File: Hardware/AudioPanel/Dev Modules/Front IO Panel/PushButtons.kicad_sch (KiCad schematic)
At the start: 80 parts, among them CN501 4x 10nF, CN502 4x 10nF, CN503 4x 10nF, U501 74HC14, U502 74HC14, U503 74HC14, U504 74HC14, U505 74HC14, U506 74HC14, U507 MCP23017_ML, U508 74HC14, U509 74HC14, U510 74HC14, U511 74HC14, U512 74HC14, U513 74HC14

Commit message: IO Panel Progress
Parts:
- removed RN501, RN502, RN503, RN504, RN505, RN506, RN507, RN508, RN509, RN510, RN511, RN512: 10k, Resistor_THT:R_Array_SIP5, symbol Device:R_Network04_Split
- removed U507: MCP23017_ML, Package_DFN_QFN:QFN-28-1EP_6x6mm_P0.65mm_EP4.25x4.25mm, symbol Interface_Expansion:MCP23017_ML
- added C102: 22uF, Libraries:Worthington_C_0603, symbol Device:C_Small
- added C103: 100nF, Libraries:Worthington_C_0402, symbol Device:C_Small
- added CN504: 4x 10nF, symbol Device:C_Network04
- added D520: SP0504BAJT, Package_TO_SOT_SMD:SOT-353_SC-70-5, symbol Power_Protection:SP0504BAJT
- added PB513, PB514, PB515, PB516: KP_Switch, symbol Switch:SW_Push
- added R102, R501: 220Ω, Libraries:Worthington_R_0402, symbol Device:R_Small_US
- added RN501, RN502, RN503, RN504, RN505: 4k7, Resistor_SMD:R_Array_Convex_4x1206, symbol Library_MicSwitcher:R_Network04_Split
- added unit 7 of U503
- added U507, U520: SN74LV165ARGYR, Libraries:RGY16_2P55X2P05, symbol Libraries:74HC165
- added U514, U515, U516, U517, U518, U519: 74HC14, symbol AudioPanelLibrary:74HC14
- C501: value 100nF -> 22uF; footprint (none) -> Libraries:Worthington_C_0603
- C502: value 10uF -> 100nF; footprint (none) -> Libraries:Worthington_C_0402
- RN513, RN514, RN515: value 47k -> 4k7
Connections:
- net PB1 is gone; now on net ~{PB1}: D501.1 (K), PB501.2, RN513.2
- net PB10 is gone; now on net ~{PB10}: D503.3 (K), PB510.2, RN515.4
- net PB11 is gone; now on net ~{PB11}: D503.4 (K), PB511.2, RN515.6
- net PB12 is gone; now on net ~{PB12}: D503.5 (K), PB512.2, RN515.8
- net PB2 is gone; now on net ~{PB2}: D501.3 (K), PB502.2, RN513.4
- net PB3 is gone; now on net ~{PB3}: D501.4 (K), PB503.2, RN513.6
- net PB4 is gone; now on net ~{PB4}: D501.5 (K), PB504.2, RN513.8
- net PB5 is gone; now on net ~{PB5}: D502.1 (K), PB505.2, RN514.2
- net PB6 is gone; now on net ~{PB6}: D502.3 (K), PB506.2, RN514.4
- net PB7 is gone; now on net ~{PB7}: D502.4 (K), PB507.2, RN514.6
- net PB8 is gone; now on net ~{PB8}: D502.5 (K), PB508.2, RN514.8
- net PB9 is gone; now on net ~{PB9}: D503.1 (K), PB509.2, RN515.2
- net GND: now also C102.2, C103.2, CN504.1 (common), D520.2 (A), PB513.1, PB514.1, PB515.1, PB516.1, R102.2, U503.7 (GND), U507.8 (GND), U520.8 (GND)
- net VDD: now also C102.1, C103.1, RN505.1, RN505.3, RN505.5, RN505.7, U503.14 (VCC), U507.16 (VCC), U520.16 (VCC)
- net ~{PB10}: now also RN503.3; no longer U511.2
- net ~{PB11}: now also RN503.5; no longer U512.2
- net ~{PB12}: now also RN503.7; no longer U513.2
- net ~{PB1}: now also RN501.1; no longer U501.2
- net ~{PB2}: now also RN501.3; no longer U502.2
- net ~{PB3}: now also RN501.5; no longer U503.2
- net ~{PB4}: now also RN501.7; no longer U504.2
- net ~{PB5}: now also RN502.1; no longer U505.2
- net ~{PB6}: now also RN502.3; no longer U506.2
- net ~{PB7}: now also RN502.5; no longer U508.2
- net ~{PB8}: now also RN502.7; no longer U509.2
- net ~{PB9}: now also RN503.1; no longer U510.2
- net at CN502.2 (C1), U505.1: now also RN502.2
- net at CN503.2 (C1), U510.1: now also RN503.2
- net at CN503.3 (C2), U511.1: now also RN503.4
- net at CN503.4 (C3), U512.1: now also RN503.6
- net at CN503.5 (C4), U513.1: now also RN503.8
- net at D519.1 (DOUT): now also R102.1
- net at CN501.5 (C4), U504.1: now also RN501.8
- net at CN501.4 (C3), U503.1: now also RN501.6
- net at CN501.2 (C1), U501.1: now also RN501.2
- net at CN502.5 (C4), U509.1: now also RN502.8
- net at CN501.3 (C2), U502.1: now also RN501.4
- net at CN502.3 (C2), U506.1: now also RN502.4
- net at D504.3 (DIN): now also R501.2
- net at CN502.4 (C3), U508.1: now also RN502.6
- new net: CN504.2 (C1), RN504.2, U514.1
- new net: U507.3 (E), U514.2
- new net: U505.2, U520.3 (E)
- new net: CN504.3 (C2), RN504.4, U515.1
- new net: U504.2, U520.14 (D)
- new net: CN504.4 (C3), RN504.6, U516.1
- new net: U507.5 (G), U516.2
- new net: U503.2, U520.13 (C)
- new net: U501.2, U520.11 (A)
- new net: U502.2, U520.12 (B)
- new net: U506.2, U520.4 (F)
- new net: U508.2, U520.5 (G)
- new net: U509.2, U520.6 (H)
- new net: U507.10 (SER), U520.9 (QH)
- new net: U507.14 (D), U513.2
- new net: U507.11 (A), U510.2
- new net: U507.4 (F), U515.2
- new net: CN504.5 (C4), RN504.8, U517.1
- new net: U507.13 (C), U512.2
- new net: U507.6 (H), U517.2
- new net: U507.12 (B), U511.2
- new net CLOCK: U507.2 (CLK), U520.2 (CLK)
- new net LED_IN: R501.1
- new net PISO_PARALLEL_LOAD: U507.1 (SH/~{LD}), U520.1 (SH/~{LD})
- new net PISO_SERIAL_IN: U520.10 (SER)
- new net PISO_SERIAL_OUT: U507.9 (QH)
- new net PISO_~{INPUT_EN}: U507.15 (~{CE}), U520.15 (~{CE})
- new net ~{PB13}: D520.1 (K), PB513.2, RN504.1, RN505.2
- new net ~{PB14}: D520.3 (K), PB514.2, RN504.3, RN505.4
- new net ~{PB15}: D520.4 (K), PB515.2, RN504.5, RN505.6
- new net ~{PB16}: D520.5 (K), PB516.2, RN504.7, RN505.8
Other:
- note added: "165-A"
- note added: "165-B"
- moved on the sheet: C503, C504, C505, C506, C507, C508, C509, C510, C511, C512, C513, C514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

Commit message: Work on front control panel
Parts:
- removed CN501, CN502, CN503, CN504: 4x 10nF, symbol Device:C_Network04
- added C401, C403, C404, C405, C406, C407, C408, C409, C410, C411, C412, C413, C414, C415, C416, C417: 100nF, Libraries:Worthington_C_0402, symbol Device:C_Small
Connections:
- net GND: now also C401.2, C403.2, C404.2, C405.2, C406.2, C407.2, C408.2, C409.2, C410.2, C411.2, C412.2, C413.2, C414.2, C415.2, C416.2, C417.2
- net ~{PB13_T}: now reaches RN504.2, U514.1
- net ~{PB13_T}: now also C414.1
- net PB13: now reaches U507.3 (E), U514.2
- net ~{PB5_T}: now reaches RN502.2, U505.1
- net ~{PB5_T}: now also C406.1
- net PB5: now reaches U505.2, U520.3 (E)
- net ~{PB9_T}: now reaches RN503.2, U510.1
- net ~{PB9_T}: now also C410.1
- net ~{PB10_T}: now reaches RN503.4, U511.1
- net ~{PB10_T}: now also C411.1
- net ~{PB11_T}: now reaches RN503.6, U512.1
- net ~{PB11_T}: now also C412.1
- net ~{PB12_T}: now reaches RN503.8, U513.1
- net ~{PB12_T}: now also C413.1
- net ~{PB14_T}: now reaches RN504.4, U515.1
- net ~{PB14_T}: now also C415.1
- net ~{PB6_T}: now reaches RN502.4, U506.1
- net ~{PB6_T}: now also C407.1
- net ~{PB4_T}: now reaches RN501.8, U504.1
- net ~{PB4_T}: now also C405.1
- net PB4: now reaches U504.2, U520.14 (D)
- net ~{PB15_T}: now reaches RN504.6, U516.1
- net ~{PB15_T}: now also C416.1
- net PB15: now reaches U507.5 (G), U516.2
- net ~{PB3_T}: now reaches RN501.6, U503.1
- net ~{PB3_T}: now also C404.1
- net PB3: now reaches U503.2, U520.13 (C)
- net PB1: now reaches U501.2, U520.11 (A)
- net PB2: now reaches U502.2, U520.12 (B)
- net PB6: now reaches U506.2, U520.4 (F)
- net PB7: now reaches U508.2, U520.5 (G)
- net PB8: now reaches U509.2, U520.6 (H)
- net PB12: now reaches U507.14 (D), U513.2
- net ~{PB1_T}: now reaches RN501.2, U501.1
- net ~{PB1_T}: now also C401.1
- net PB9: now reaches U507.11 (A), U510.2
- net ~{PB8_T}: now reaches RN502.8, U509.1
- net ~{PB8_T}: now also C409.1
- net PB14: now reaches U507.4 (F), U515.2
- net ~{PB16_T}: now reaches RN504.8, U517.1
- net ~{PB16_T}: now also C417.1
- net ~{PB2_T}: now reaches RN501.4, U502.1
- net ~{PB2_T}: now also C403.1
- net PB11: now reaches U507.13 (C), U512.2
- net PB16: now reaches U507.6 (H), U517.2
- net PB10: now reaches U507.12 (B), U511.2
- net ~{PB7_T}: now reaches RN502.6, U508.1
- net ~{PB7_T}: now also C408.1
- no-connect marks 0 -> 4
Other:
- moved on the sheet: C102, C103, C501, C502, U501A, U507, U508A, U514A, U520

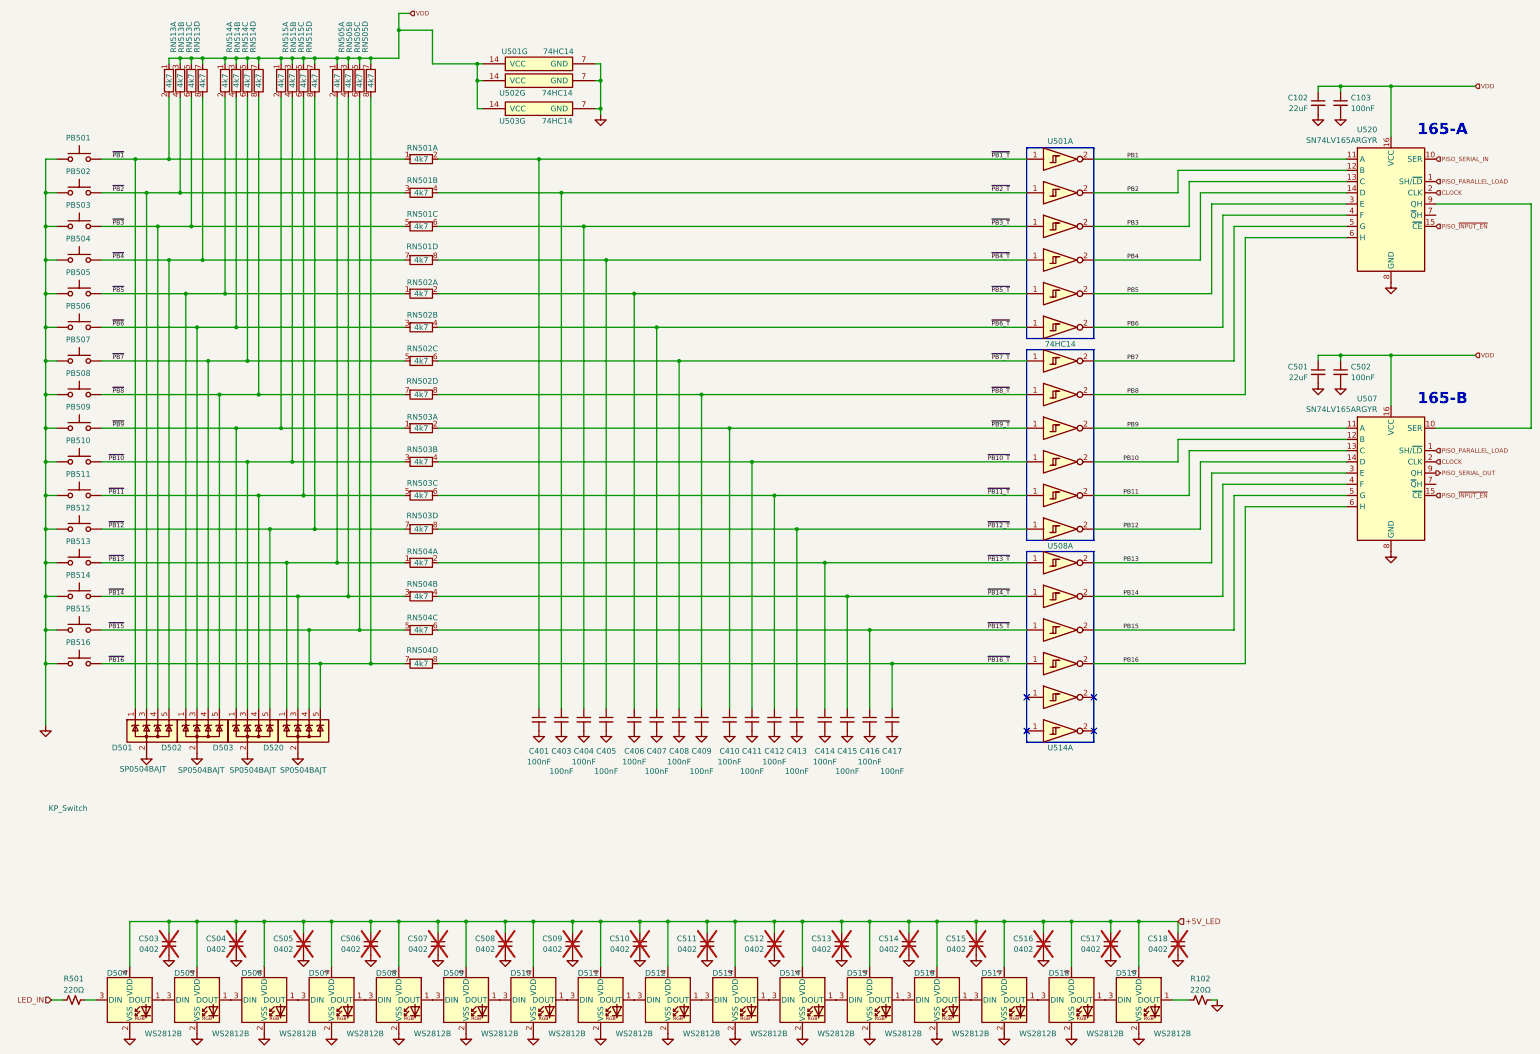
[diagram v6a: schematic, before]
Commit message: Fixed some footprints
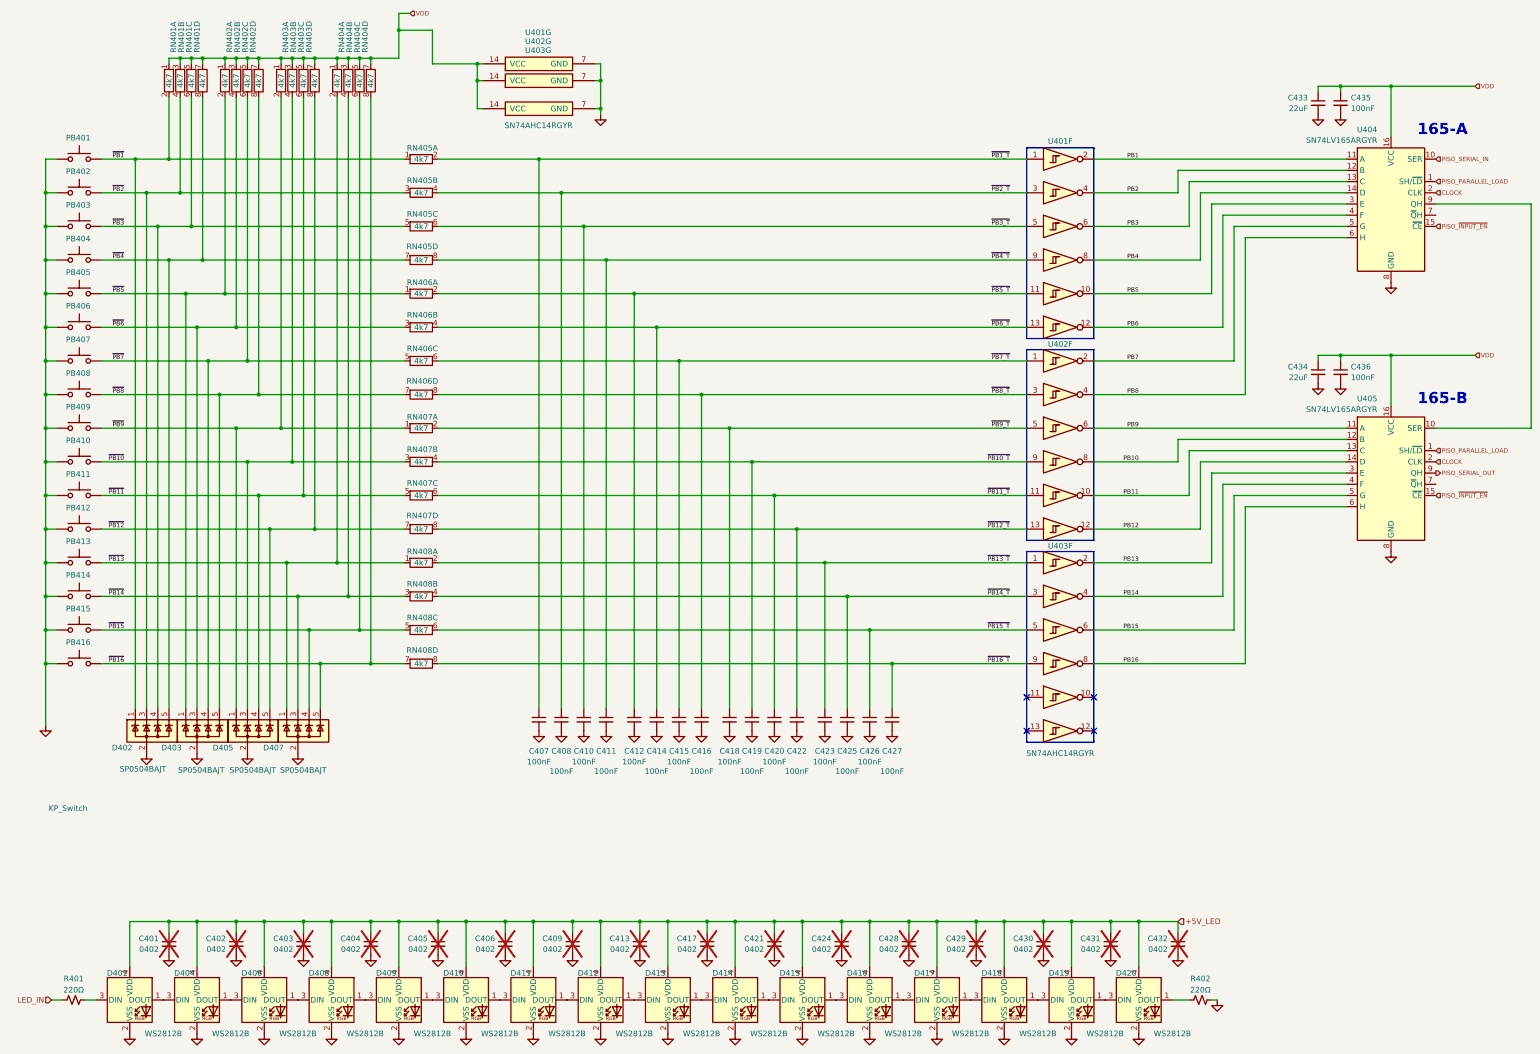
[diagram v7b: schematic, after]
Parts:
- removed unit 1 of U501
- removed unit 1 of U502
- removed unit 1 of U503
- removed U504, U505, U506, U508, U509, U510, U511, U512, U513, U514, U515, U516, U517, U518, U519: 74HC14, symbol AudioPanelLibrary:74HC14
- added unit 2 of U401
- added unit 4 of U401
- added unit 3 of U401
- added unit 6 of U401
- added unit 5 of U401
- added unit 1 of U401
- added unit 4 of U402
- added unit 3 of U402
- added unit 6 of U402
- added unit 5 of U402
- added unit 2 of U402
- added unit 1 of U402
- added unit 5 of U403
- added unit 4 of U403
- added unit 2 of U403
- added unit 6 of U403
- added unit 3 of U403
- added unit 1 of U403
- C401: renamed from C503; footprint Capacitor_SMD:C_0402_1005Metric -> Libraries:Worthington_C_0402
- C402: renamed from C504; footprint Capacitor_SMD:C_0402_1005Metric -> Libraries:Worthington_C_0402
- C403: renamed from C505; footprint Capacitor_SMD:C_0402_1005Metric -> Libraries:Worthington_C_0402
- C404: renamed from C506; footprint Capacitor_SMD:C_0402_1005Metric -> Libraries:Worthington_C_0402
- C405: renamed from C507; footprint Capacitor_SMD:C_0402_1005Metric -> Libraries:Worthington_C_0402
- C406: renamed from C508; footprint Capacitor_SMD:C_0402_1005Metric -> Libraries:Worthington_C_0402
- C409: renamed from C509; footprint Capacitor_SMD:C_0402_1005Metric -> Libraries:Worthington_C_0402
- C413: renamed from C510; footprint Capacitor_SMD:C_0402_1005Metric -> Libraries:Worthington_C_0402
- C417: renamed from C511; footprint Capacitor_SMD:C_0402_1005Metric -> Libraries:Worthington_C_0402
- C421: renamed from C512; footprint Capacitor_SMD:C_0402_1005Metric -> Libraries:Worthington_C_0402
- C424: renamed from C513; footprint Capacitor_SMD:C_0402_1005Metric -> Libraries:Worthington_C_0402
- C428: renamed from C514; footprint Capacitor_SMD:C_0402_1005Metric -> Libraries:Worthington_C_0402
- C429: renamed from C515; footprint Capacitor_SMD:C_0402_1005Metric -> Libraries:Worthington_C_0402
- C430: renamed from C516; footprint Capacitor_SMD:C_0402_1005Metric -> Libraries:Worthington_C_0402
- C431: renamed from C517; footprint Capacitor_SMD:C_0402_1005Metric -> Libraries:Worthington_C_0402
- C432: renamed from C518; footprint Capacitor_SMD:C_0402_1005Metric -> Libraries:Worthington_C_0402
- U401: renamed from U501; value 74HC14 -> SN74AHC14RGYR; footprint (none) -> Libraries:RGY14_2P05X2P05
- U402: renamed from U502; value 74HC14 -> SN74AHC14RGYR; footprint (none) -> Libraries:RGY14_2P05X2P05
- U403: renamed from U503; value 74HC14 -> SN74AHC14RGYR; footprint (none) -> Libraries:RGY14_2P05X2P05
- renumbered C401 to C407, C403 to C408, C404 to C410, C405 to C411, C406 to C412, C407 to C414, C408 to C415, C409 to C416, C410 to C418, C411 to C419, C412 to C420, C413 to C422, C414 to C423, C415 to C425, C416 to C426, C417 to C427, C102 to C433, C501 to C434, C103 to C435, C502 to C436, D504 to D401, D501 to D402, D502 to D403, D505 to D404, D503 to D405, D506 to D406, D520 to D407, D507 to D408, D508 to D409, D509 to D410, D510 to D411, D511 to D412, D512 to D413, D513 to D414, D514 to D415, D515 to D416, D516 to D417, D517 to D418, D518 to D419, D519 to D420, PB501 to PB401, PB502 to PB402, PB503 to PB403, PB504 to PB404, PB505 to PB405, PB506 to PB406, PB507 to PB407, PB508 to PB408, PB509 to PB409, PB510 to PB410, PB511 to PB411, PB512 to PB412, PB513 to PB413, PB514 to PB414, PB515 to PB415, PB516 to PB416, R501 to R401, R102 to R402, RN513 to RN401, RN514 to RN402, RN515 to RN403, RN505 to RN404, RN501 to RN405, RN502 to RN406, RN503 to RN407, RN504 to RN408, U520 to U404, U507 to U405
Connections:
- net PB1: now also U401.2
- net PB10: now also U402.8
- net PB11: now also U402.10
- net PB12: now also U402.12
- net PB13: now also U403.2
- net PB14: now also U403.4
- net PB15: now also U403.6
- net PB16: now also U403.8
- net PB2: now also U401.4
- net PB3: now also U401.6
- net PB4: now also U401.8
- net PB5: now also U401.10
- net PB6: now also U401.12
- net PB7: now also U402.2
- net PB8: now also U402.4
- net PB9: now also U402.6
- net ~{PB10_T}: now also U402.9
- net ~{PB11_T}: now also U402.11
- net ~{PB12_T}: now also U402.13
- net ~{PB13_T}: now also U403.1
- net ~{PB14_T}: now also U403.3
- net ~{PB15_T}: now also U403.5
- net ~{PB16_T}: now also U403.9
- net ~{PB1_T}: now also U401.1
- net ~{PB2_T}: now also U401.3
- net ~{PB3_T}: now also U401.5
- net ~{PB4_T}: now also U401.9
- net ~{PB5_T}: now also U401.11
- net ~{PB6_T}: now also U401.13
- net ~{PB7_T}: now also U402.1
- net ~{PB8_T}: now also U402.3
- net ~{PB9_T}: now also U402.5
